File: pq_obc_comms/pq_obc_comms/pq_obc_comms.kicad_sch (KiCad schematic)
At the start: 71 parts, among them J1 Conn_01x10, J2 Conn_01x10, J3 Conn_01x10, J4 Conn_01x10, J6 U.FL, U1 STM32L476RGTx, U2 SX1262IMLTRT, U3 BD2232G-GTR, U4 BD2232G-GTR, U5 BGS12PL6E6327XTSA1, U6 BD2232G-GTR, U7 BD2232G-GTR, X1 ECS-120-18-33-JEM-TR3, X2 FA-128_32.0000MF20X-K5, X3 ABS09-32.768KHZ-7-T

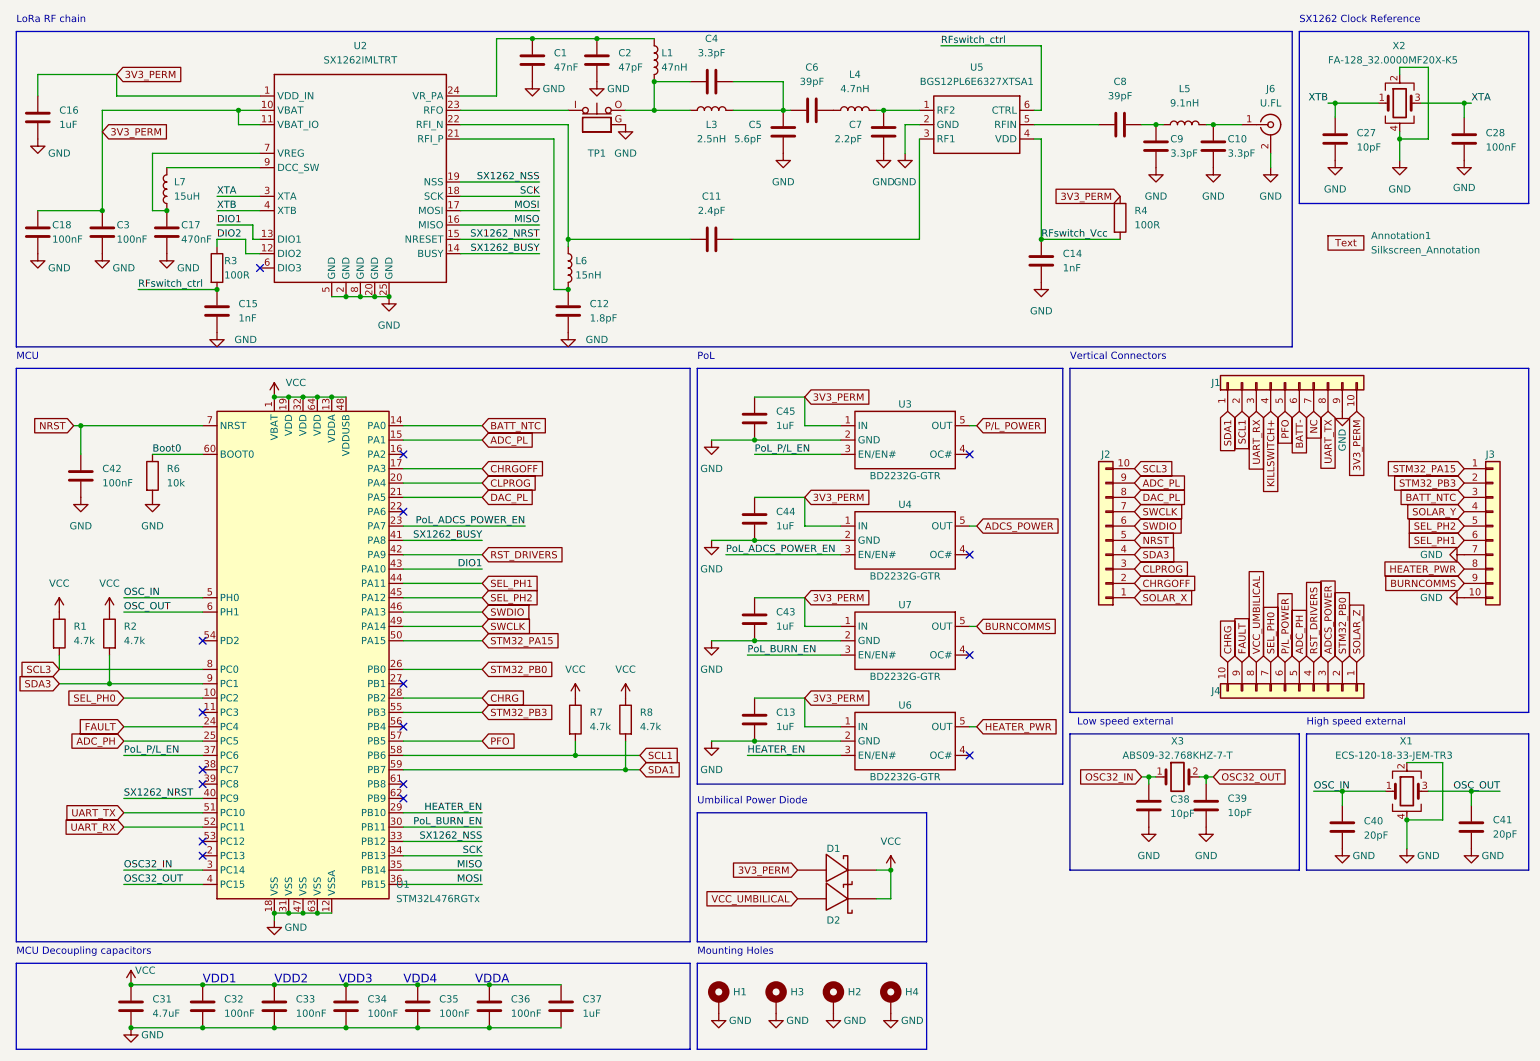
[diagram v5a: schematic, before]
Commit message: Symbol path corrections, X1 crystal mirror correction, J2&J3&J4 name flip PCB
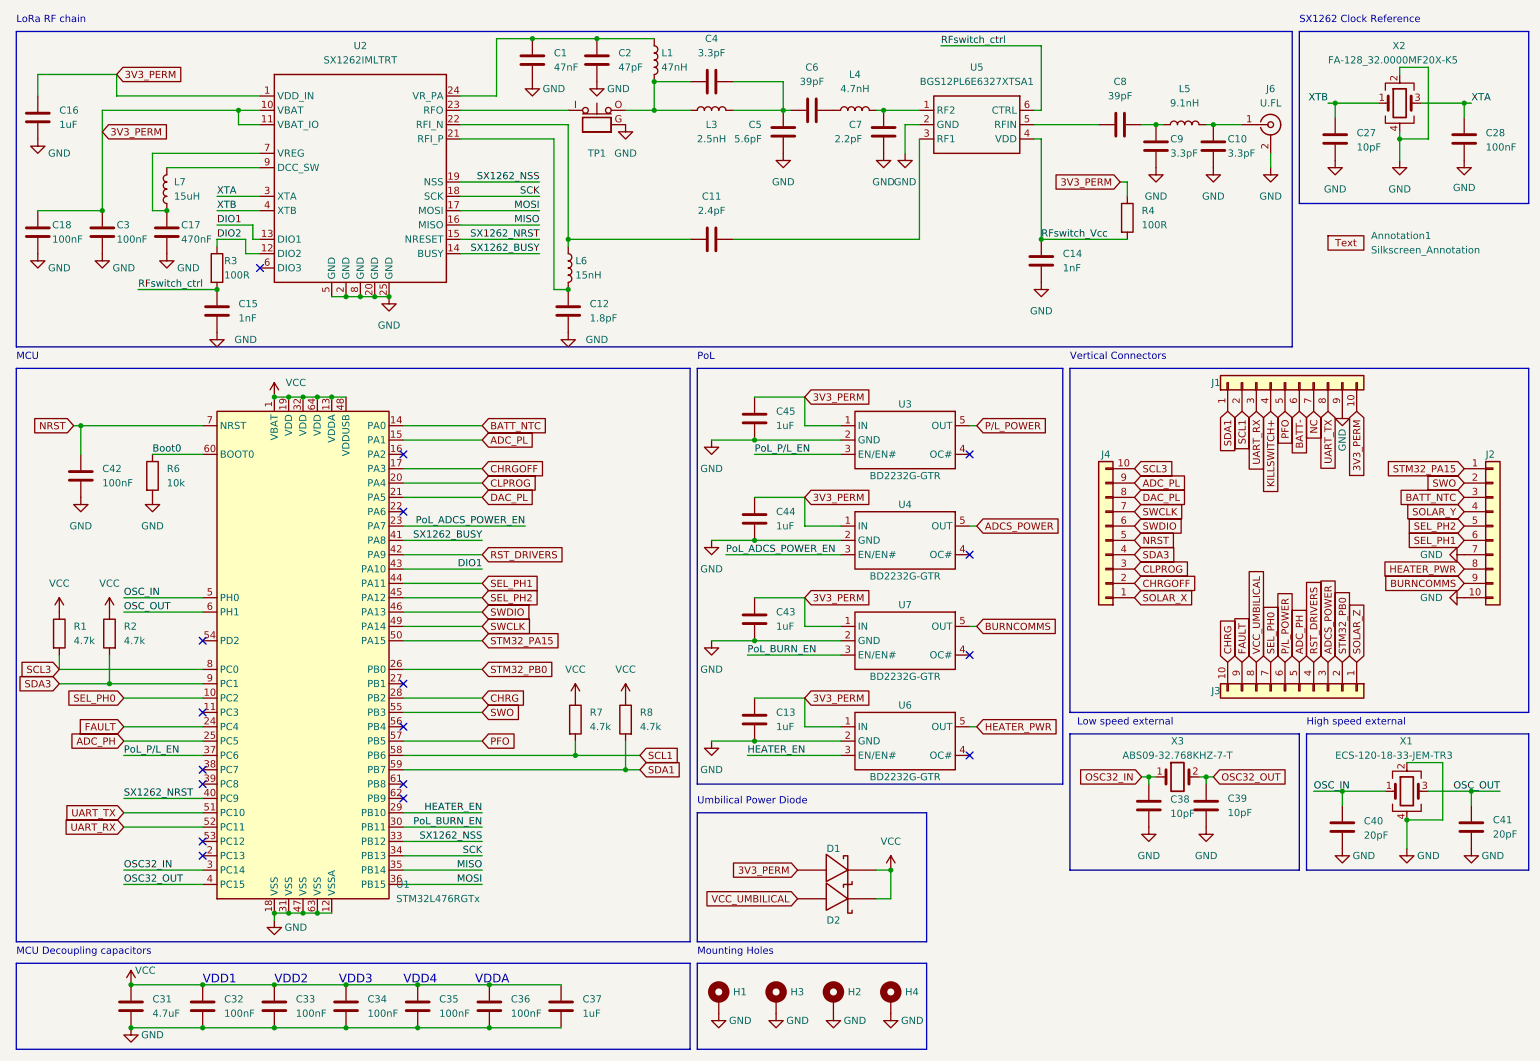
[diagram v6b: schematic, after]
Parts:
- Annotation1: footprint -nsl_symbols:Bike -> symbols-nsl:Bike
- D1, D2: footprint -nsl_passive:RBS1LAM40ATR_Schottky -> passive-nsl:RBS1LAM40ATR_Schottky
- J1: footprint -nsl_connector:SLW-110-01 -> connector-nsl:SLW-110-01
- J2: renamed from J3; footprint -nsl_connector:SLW-110-01 -> connector-nsl:SLW-110-01
- J3: renamed from J4; footprint -nsl_connector:SLW-110-01 -> connector-nsl:SLW-110-01
- J4: renamed from J2; footprint -nsl_connector:SLW-110-01 -> connector-nsl:SLW-110-01
- TP1: footprint -nsl_connector:CoaxialSwitch_Hirose_MS-156C3_Horizontal -> connector-nsl:CoaxialSwitch_Hirose_MS-156C3_Horizontal
- U5: footprint -nsl_rf:PG-TSLP-6-4 -> rf-nsl:PG-TSLP-6-4
- X1: footprint miscelaneous-nsl:ECX-32 -> miscelaneous-nsl:ECS-120-18-33
- X2: footprint -nsl_miscellaneous:EPSON_FA128 -> miscelaneous-nsl:EPSON_FA128
- X3: footprint -nsl_miscellaneous:ABS09 -> miscelaneous-nsl:ABS09
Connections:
- net STM32_PB3 renamed SWO
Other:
- moved on the sheet: R4
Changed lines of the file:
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@@
     (stroke (width 0) (type default))
   )
-  (wire (pts (xy 195.58 53.34) (xy 209.55 53.34))
+  (wire (pts (xy 195.58 53.34) (xy 210.82 53.34))
     (stroke (width 0) (type default))
   )
@@
     (stroke (width 0) (type default))
   )
+  (wire (pts (xy 210.82 43.18) (xy 209.55 43.18))
+    (stroke (width 0) (type default))
+  )
   (polyline (pts (xy 240.03 72.39) (xy 240.03 16.51))
     (stroke (width 0) (type default))
@@
     (stroke (width 0) (type default))
   )
+  (wire (pts (xy 210.82 43.18) (xy 210.82 45.72))
+    (stroke (width 0) (type default))
+  )
   (polyline (pts (xy 133.35 177.8) (xy 133.35 76.2))
     (stroke (width 0) (type default))
@@
     )
   )
+  (global_label "SWO" (shape input) (at 96.52 137.16 0) (fields_autoplaced)
+    (effects (font (size 1.27 1.27)) (justify left))
+    (property "Intersheetrefs" "${INTERSHEET_REFS}" (at 103.4966 137.16 0)
+      (effects (font (size 1.27 1.27)) (justify left) hide)
+    )
+  )
   (global_label "SDA3" (shape input) (at 21.59 132.08 180) (fields_autoplaced)
     (effects (font (size 1.27 1.27)) (justify right))
@@
     )
   )
-  (global_label "3V3_PERM" (shape input) (at 209.55 45.72 180) (fields_autoplaced)
+  (global_label "3V3_PERM" (shape input) (at 209.55 43.18 180) (fields_autoplaced)
     (effects (font (size 1.27 1.27)) (justify right))
-    (property "Intersheetrefs" "${INTERSHEET_REFS}" (at 197.0286 45.72 0)
+    (property "Intersheetrefs" "${INTERSHEET_REFS}" (at 197.0286 43.18 0)
       (effects (font (size 1.27 1.27)) (justify right) hide)
     )
@@
     )
   )
-  (global_label "STM32_PB3" (shape input) (at 96.52 137.16 0) (fields_autoplaced)
-    (effects (font (size 1.27 1.27)) (justify left))
-    (property "Intersheetrefs" "${INTERSHEET_REFS}" (at 109.6979 137.0806 0)
-      (effects (font (size 1.27 1.27)) (justify left) hide)
-    )
-  )
   (global_label "CHRGOFF" (shape input) (at 212.09 114.3 0) (fields_autoplaced)
     (effects (font (size 1.27 1.27)) (justify left))
@@
     )
   )
-  (global_label "STM32_PB3" (shape input) (at 270.51 96.52 180) (fields_autoplaced)
+  (global_label "SWO" (shape input) (at 270.51 96.52 180) (fields_autoplaced)
     (effects (font (size 1.27 1.27)) (justify right))
-    (property "Intersheetrefs" "${INTERSHEET_REFS}" (at 257.3321 96.4406 0)
+    (property "Intersheetrefs" "${INTERSHEET_REFS}" (at 263.5334 96.52 0)
       (effects (font (size 1.27 1.27)) (justify right) hide)
     )
@@
       (effects (font (size 1.27 1.27)) (justify left))
     )
-    (property "Footprint" "-nsl_symbols:Bike" (at 247.65 59.69 0)
+    (property "Footprint" "symbols-nsl:Bike" (at 247.65 59.69 0)
       (effects (font (size 1.27 1.27)) hide)
     )
@@
       (effects (font (size 1.27 1.27)))
     )
-    (property "Footprint" "-nsl_rf:PG-TSLP-6-4" (at 182.88 39.37 0)
+    (property "Footprint" "rf-nsl:PG-TSLP-6-4" (at 182.88 39.37 0)
       (effects (font (size 1.27 1.27)) hide)
     )
@@
     )
   )
-  (symbol (lib_id "Device:R") (at 209.55 49.53 0) (unit 1)
+  (symbol (lib_id "Device:R") (at 210.82 49.53 0) (unit 1)
     (in_bom yes) (on_board yes) (dnp no) (fields_autoplaced)
-    (property "Reference" "R4" (at 212.09 48.2599 0)
+    (property "Reference" "R4" (at 213.36 48.2599 0)
       (effects (font (size 1.27 1.27)) (justify left))
     )
-    (property "Value" "100R" (at 212.09 50.7999 0)
+    (property "Value" "100R" (at 213.36 50.7999 0)
       (effects (font (size 1.27 1.27)) (justify left))
     )
-    (property "Footprint" "Resistor_SMD:R_0603_1608Metric" (at 207.772 49.53 90)
+    (property "Footprint" "Resistor_SMD:R_0603_1608Metric" (at 209.042 49.53 90)
       (effects (font (size 1.27 1.27)) hide)
     )
-    (property "Datasheet" "~" (at 209.55 49.53 0)
+    (property "Datasheet" "~" (at 210.82 49.53 0)
       (effects (font (size 1.27 1.27)) hide)
     )
-    (property "CONTRIBUTOR" "danielCOMMS" (at 208.28 46.99 0)
+    (property "CONTRIBUTOR" "danielCOMMS" (at 209.55 46.99 0)
       (effects (font (size 1.27 1.27)) (justify left bottom) hide)
     )
-    (property "SPICEPRE" "R" (at 209.55 49.53 0)
+    (property "SPICEPRE" "R" (at 210.82 49.53 0)
       (effects (font (size 1.27 1.27)) (justify left bottom) hide)
     )
-    (property "SPICESYMBOLNAME" "RC0603JR-07100RL" (at 209.55 49.53 0)
+    (property "SPICESYMBOLNAME" "RC0603JR-07100RL" (at 210.82 49.53 0)
       (effects (font (size 1.27 1.27)) (justify left bottom) hide)
     )
-    (property "BOM_MANUFACTURER PART" "" (at 209.55 49.53 0)
+    (property "BOM_MANUFACTURER PART" "" (at 210.82 49.53 0)
       (effects (font (size 1.27 1.27)) (justify left bottom) hide)
     )
-    (property "Manufacturer 1" "YAGEO" (at 209.55 49.53 0)
+    (property "Manufacturer 1" "YAGEO" (at 210.82 49.53 0)
       (effects (font (size 1.27 1.27)) hide)
     )
-    (property "Manufacturer Part Number 1" "RC0603JR-07100RL" (at 209.55 49.53 0)
+    (property "Manufacturer Part Number 1" "RC0603JR-07100RL" (at 210.82 49.53 0)
       (effects (font (size 1.27 1.27)) hide)
     )
-    (property "Supplier 1" "Mouser" (at 209.55 49.53 0)
+    (property "Supplier 1" "Mouser" (at 210.82 49.53 0)
       (effects (font (size 1.27 1.27)) hide)
     )
-    (property "Supplier Part Number 1" "603-RC0603JR-07100RL" (at 209.55 49.53 0)
+    (property "Supplier Part Number 1" "603-RC0603JR-07100RL" (at 210.82 49.53 0)
       (effects (font (size 1.27 1.27)) hide)
     )
@@
   (symbol (lib_id "-nsl_connector:SLW-110-01") (at 240.03 133.35 270) (unit 1)
     (in_bom yes) (on_board yes) (dnp no)
-    (property "Reference" "J4" (at 227.33 133.35 90)
+    (property "Reference" "J3" (at 227.33 133.35 90)
       (effects (font (size 1.27 1.27)) (justify right))
     )
@@
       (effects (font (size 1.27 1.27)) hide)
     )
-    (property "Footprint" "-nsl_connector:SLW-110-01" (at 241.046 136.144 90)
+    (property "Footprint" "connector-nsl:SLW-110-01" (at 241.046 136.144 90)
       (effects (font (size 1.27 1.27)) hide)
     )
@@
       (project "pq_obc_comms"
         (path "/147266d0-f330-479a-98d7-fb2f63528b30"
-          (reference "J4") (unit 1)
+          (reference "J3") (unit 1)
         )
       )
@@
   (symbol (lib_id "-nsl_connector:SLW-110-01") (at 207.01 105.41 180) (unit 1)
     (in_bom yes) (on_board yes) (dnp no)
-    (property "Reference" "J2" (at 207.01 91.44 0)
+    (property "Reference" "J4" (at 207.01 91.44 0)
       (effects (font (size 1.27 1.27)))
     )
@@
       (effects (font (size 1.27 1.27)) hide)
     )
-    (property "Footprint" "-nsl_connector:SLW-110-01" (at 204.216 106.426 90)
+    (property "Footprint" "connector-nsl:SLW-110-01" (at 204.216 106.426 90)
       (effects (font (size 1.27 1.27)) hide)
     )
@@
       (project "pq_obc_comms"
         (path "/147266d0-f330-479a-98d7-fb2f63528b30"
-          (reference "J2") (unit 1)
+          (reference "J4") (unit 1)
         )
       )
@@
       (effects (font (size 1.27 1.27)) (justify left))
     )
-    (property "Footprint" "-nsl_miscellaneous:EPSON_FA128" (at 259.08 29.21 0)
+    (property "Footprint" "miscelaneous-nsl:EPSON_FA128" (at 259.08 29.21 0)
       (effects (font (size 1.27 1.27)) hide)
     )
@@
       (effects (font (size 1.27 1.27)) (justify left) hide)
     )
-    (property "Footprint" "-nsl_passive:RBS1LAM40ATR_Schottky" (at 162.56 172.72 0)
+    (property "Footprint" "passive-nsl:RBS1LAM40ATR_Schottky" (at 162.56 172.72 0)
       (effects (font (size 1.27 1.27)) hide)
     )
@@
       (effects (font (size 1.27 1.27)))
     )
-    (property "Footprint" "-nsl_miscellaneous:ABS09" (at 226.568 144.272 0)
+    (property "Footprint" "miscelaneous-nsl:ABS09" (at 226.568 144.272 0)
       (effects (font (size 1.27 1.27)) hide)
     )
@@
   (symbol (lib_id "-nsl_connector:SLW-110-01") (at 275.59 105.41 0) (unit 1)
     (in_bom yes) (on_board yes) (dnp no)
-    (property "Reference" "J3" (at 274.32 91.44 0)
+    (property "Reference" "J2" (at 274.32 91.44 0)
       (effects (font (size 1.27 1.27)) (justify left))
     )
@@
       (effects (font (size 1.27 1.27)) hide)
     )
-    (property "Footprint" "-nsl_connector:SLW-110-01" (at 278.384 104.394 90)
+    (property "Footprint" "connector-nsl:SLW-110-01" (at 278.384 104.394 90)
       (effects (font (size 1.27 1.27)) hide)
     )
@@
       (project "pq_obc_comms"
         (path "/147266d0-f330-479a-98d7-fb2f63528b30"
-          (reference "J3") (unit 1)
+          (reference "J2") (unit 1)
         )
       )
@@
       (effects (font (size 1.27 1.27)) (justify left))
     )
-    (property "Footprint" "miscelaneous-nsl:ECX-32" (at 260.35 151.13 0)
+    (property "Footprint" "miscelaneous-nsl:ECS-120-18-33" (at 260.35 151.13 0)
       (effects (font (size 1.27 1.27)) hide)
     )
@@
       (effects (font (size 1.27 1.27)) hide)
     )
-    (property "Footprint" "-nsl_connector:SLW-110-01" (at 239.014 75.946 90)
+    (property "Footprint" "connector-nsl:SLW-110-01" (at 239.014 75.946 90)
       (effects (font (size 1.27 1.27)) hide)
     )
@@
       (effects (font (size 1.27 1.27)) hide)
     )
-    (property "Footprint" "-nsl_connector:CoaxialSwitch_Hirose_MS-156C3_Horizontal" (at 116.84 36.83 0)
+    (property "Footprint" "connector-nsl:CoaxialSwitch_Hirose_MS-156C3_Horizontal" (at 116.84 36.83 0)
       (effects (font (size 1.27 1.27)) hide)
     )
@@
       (effects (font (size 1.27 1.27)) (justify left) hide)
     )
-    (property "Footprint" "-nsl_passive:RBS1LAM40ATR_Schottky" (at 162.56 167.64 0)
+    (property "Footprint" "passive-nsl:RBS1LAM40ATR_Schottky" (at 162.56 167.64 0)
       (effects (font (size 1.27 1.27)) hide)
     )

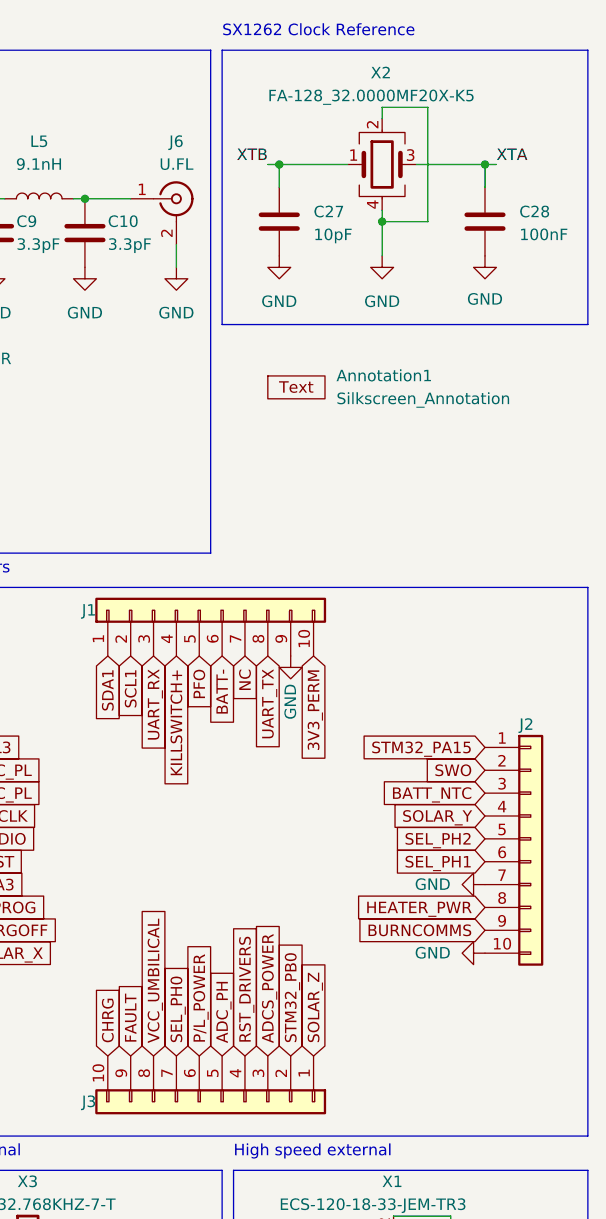
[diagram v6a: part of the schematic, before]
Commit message: delete LoRa crystal capacitors and swap SOLARZ with GND
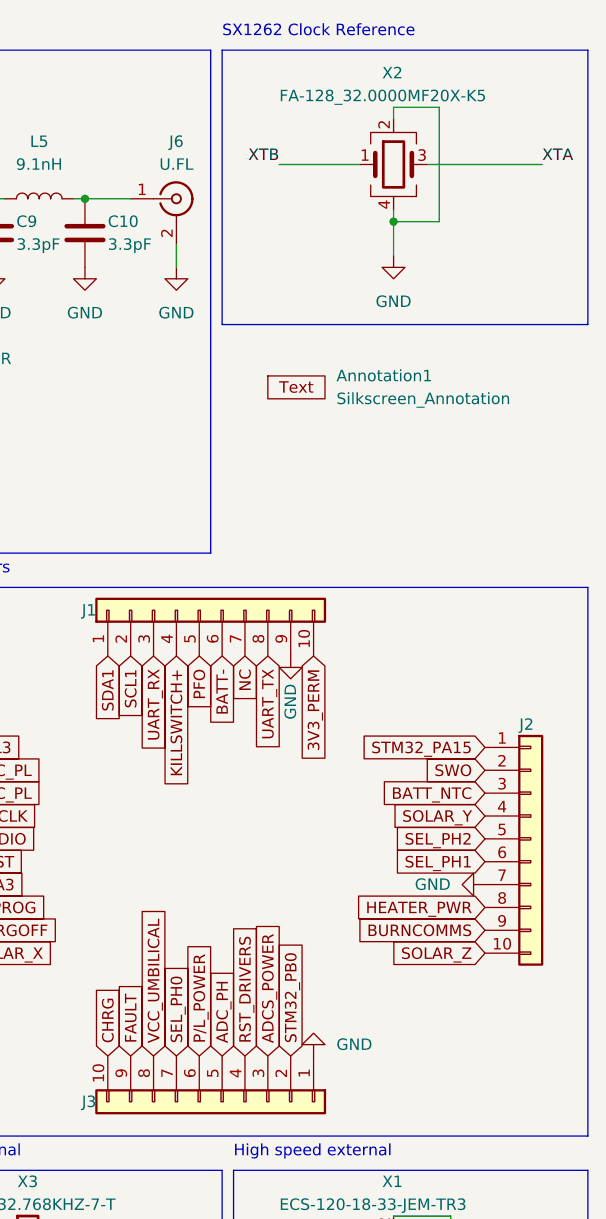
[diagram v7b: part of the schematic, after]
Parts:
- removed C27: 10pF, Capacitor_SMD:C_0603_1608Metric, symbol Device:C
- removed C28: 100nF, Capacitor_SMD:C_0603_1608Metric, symbol Device:C
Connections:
- net GND: now also J3.1; no longer J2.10
- net SOLAR_Z: now also J2.10; no longer J3.1
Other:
- moved on the sheet: X2
